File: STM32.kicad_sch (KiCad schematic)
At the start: 7 parts

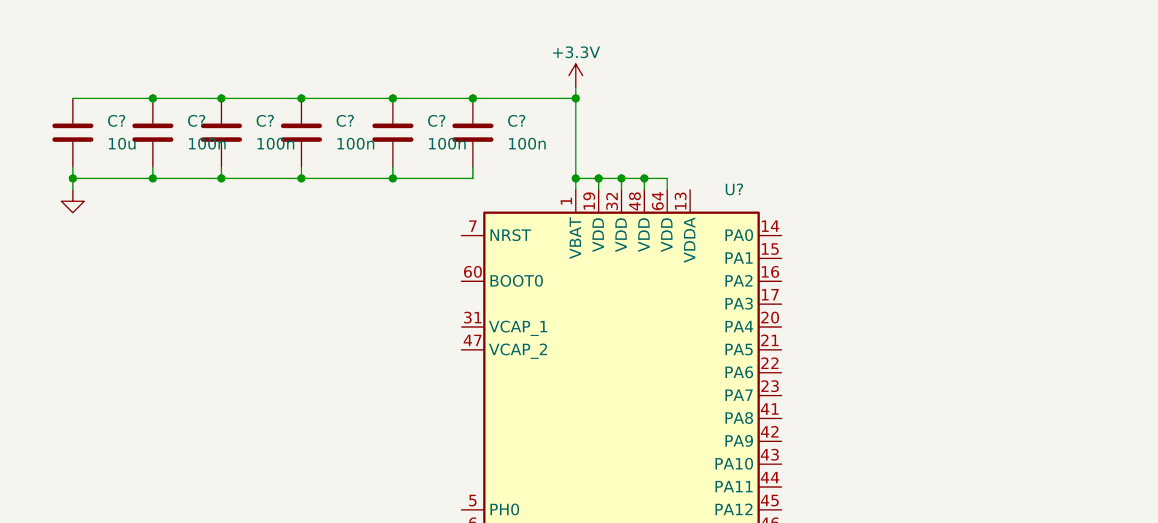
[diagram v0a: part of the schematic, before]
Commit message: update
NRST and BOOT0
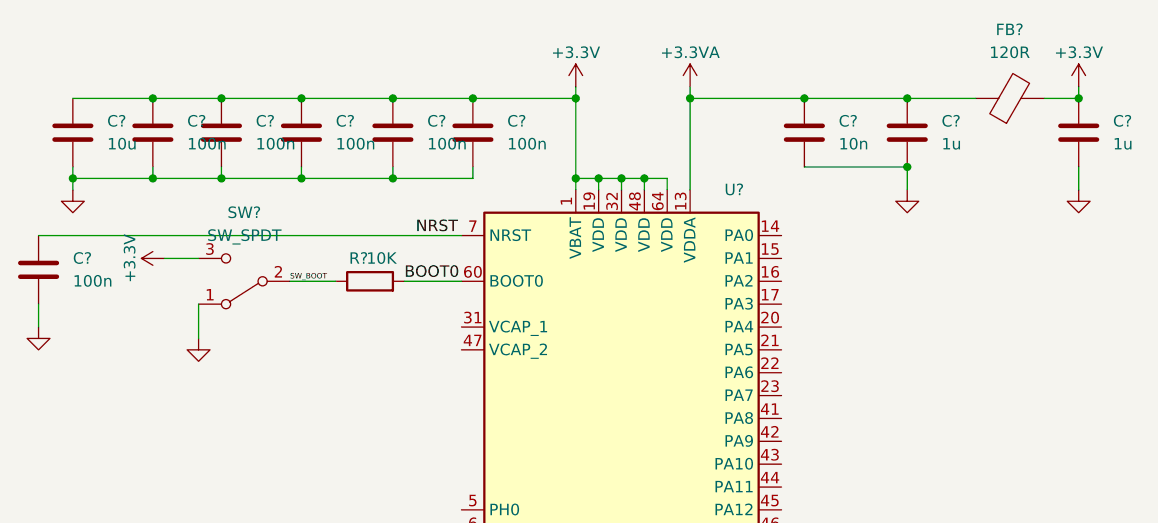
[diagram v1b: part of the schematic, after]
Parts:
- added C?: 10n, symbol Device:C
- added C? (x2): 1u, symbol Device:C
- added C?: 100n, symbol Device:C
- added FB?: 120R, symbol Device:FerriteBead
- added R?: 10K, symbol Device:R
- added SW?: SW_SPDT, symbol Switch:SW_SPDT
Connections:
- net +3.3V: now also C?.1, FB?.2, SW?.3 (C)
- net GND: now also C?.2, C?.2, C?.2, C?.2, SW?.1 (A)
- net +3.3VA: now reaches U?.13 (VDDA)
- net +3.3VA: now also C?.1, C?.1, FB?.1
- net BOOT0: now reaches U?.60 (BOOT0)
- net BOOT0: now also R?.2
- net NRST: now reaches U?.7 (NRST)
- net NRST: now also C?.1
- new net SW_BOOT: R?.1, SW?.2 (B)

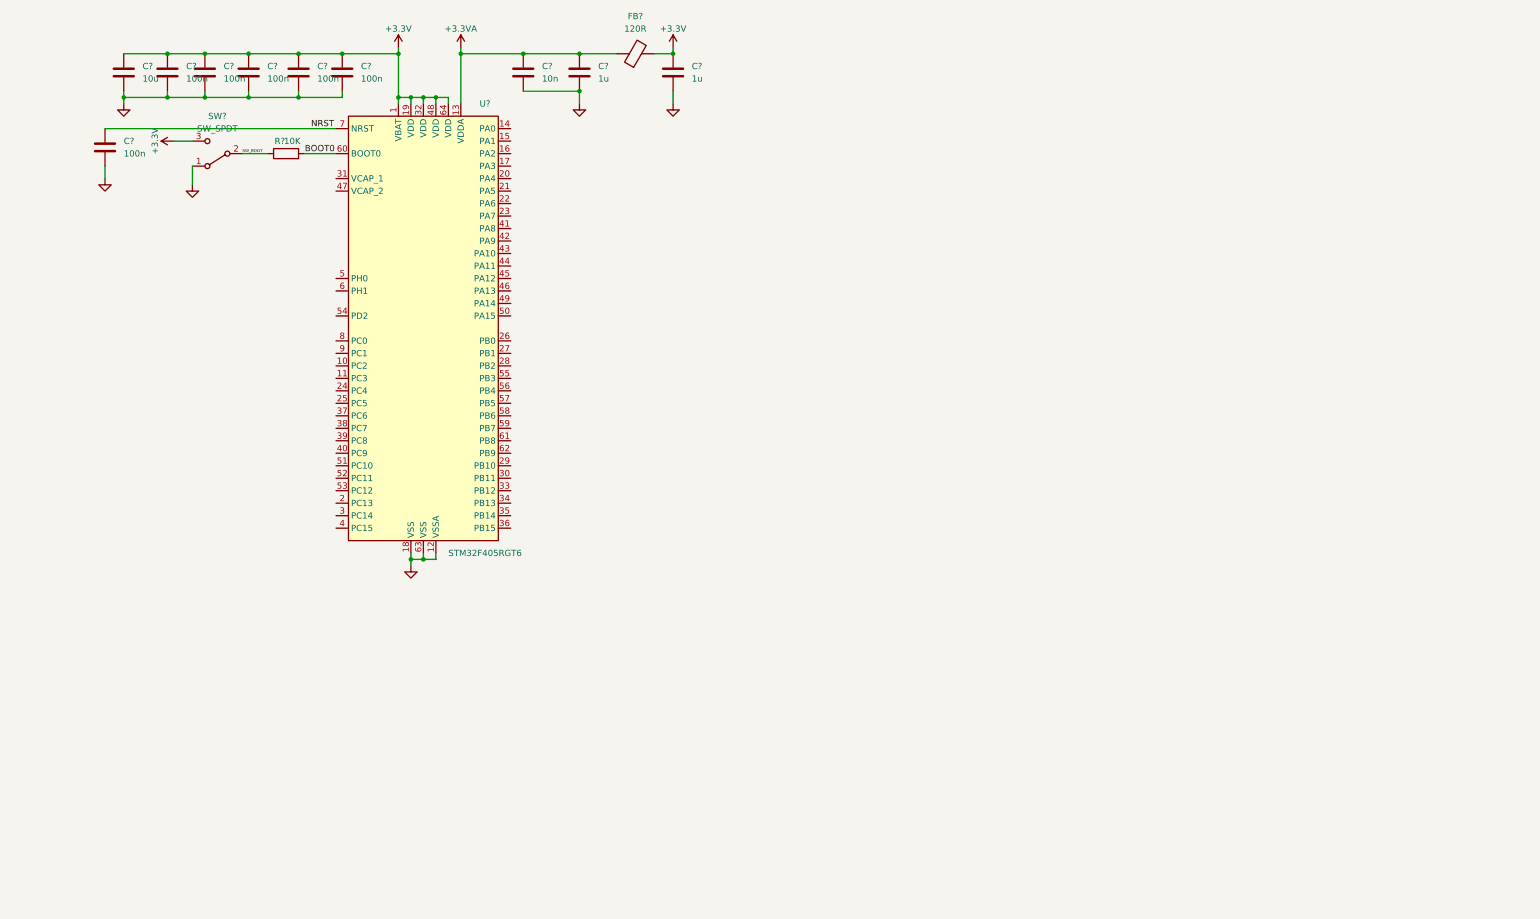
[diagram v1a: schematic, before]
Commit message: Schematics update
New files and schematics
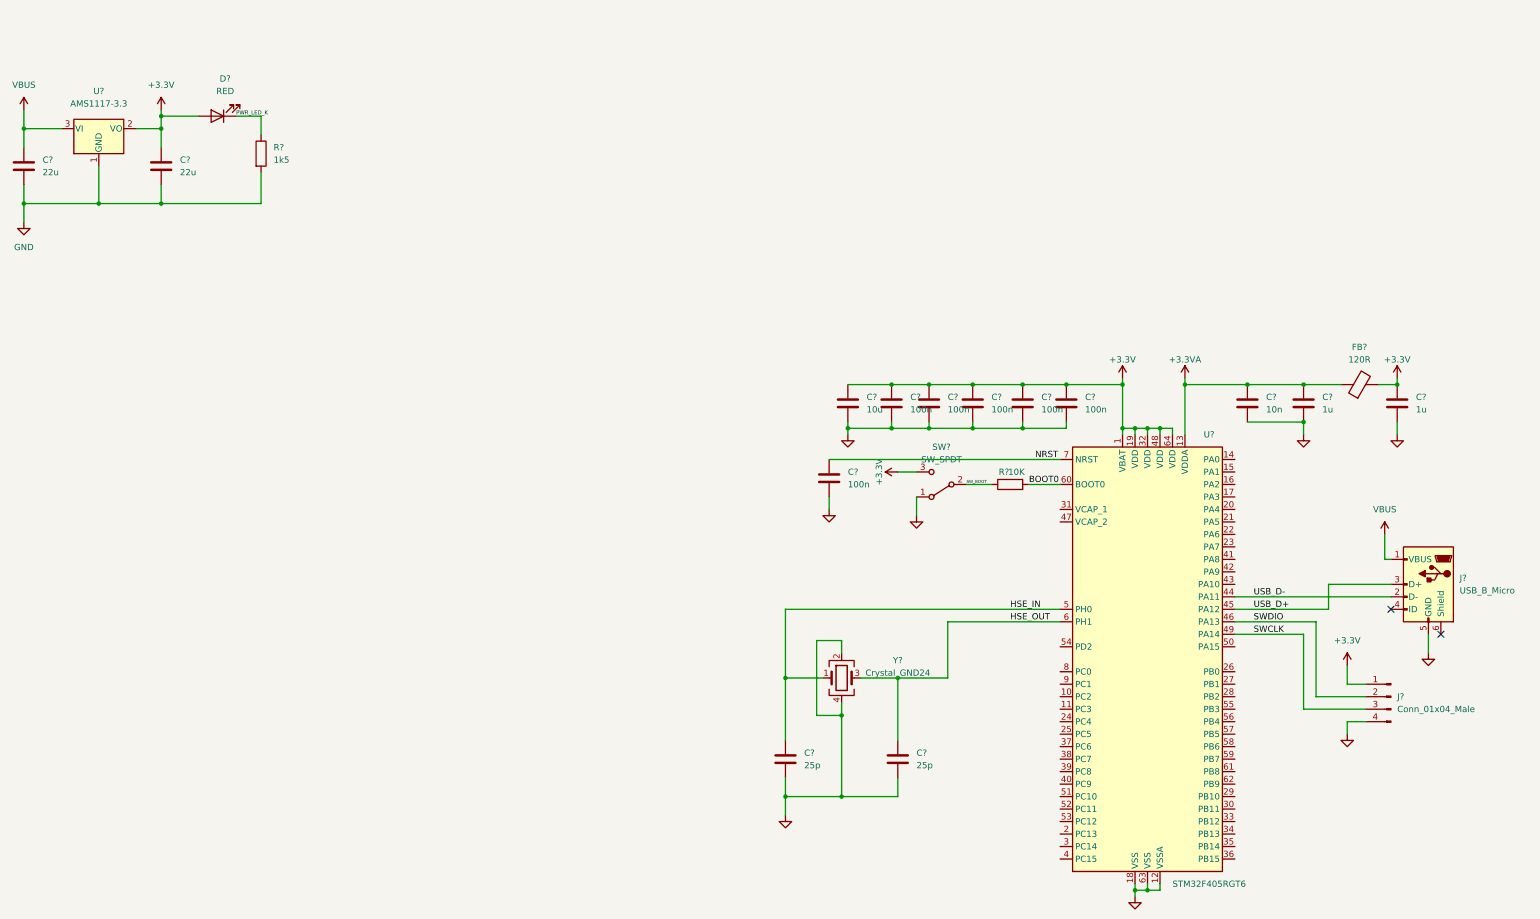
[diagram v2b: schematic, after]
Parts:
- added C? (x2): 22u, symbol Device:C
- added C? (x2): 25p, symbol Device:C
- added D?: RED, symbol Device:LED
- added J?: USB_B_Micro, symbol Connector:USB_B_Micro
- added J?: Conn_01x04_Male, symbol Connector:Conn_01x04_Male
- added R?: 1k5, symbol Device:R
- added U?: AMS1117-3.3, Package_TO_SOT_SMD:SOT-223-3_TabPin2, symbol Regulator_Linear:AMS1117-3.3
- added Y?: Crystal_GND24, symbol Device:Crystal_GND24
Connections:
- net +3.3V: now also C?.1, D?.2 (A), J?.1 (Pin_1), U?.2 (VO)
- net GND: now also C?.2, C?.2, C?.2, C?.2, J?.4 (Pin_4), J?.5 (GND), R?.2, U?.1 (GND), Y?.2, Y?.4
- net USB_D-: now reaches U?.44 (PA11)
- net USB_D-: now also J?.2 (D-)
- net USB_D+: now reaches U?.45 (PA12)
- net USB_D+: now also J?.3 (D+)
- net SWDIO: now reaches U?.46 (PA13)
- net SWDIO: now also J?.2 (Pin_2)
- net SWCLK: now reaches U?.49 (PA14)
- net SWCLK: now also J?.3 (Pin_3)
- net HSE_IN: now reaches U?.5 (PH0)
- net HSE_IN: now also C?.1, Y?.1
- net HSE_OUT: now reaches U?.6 (PH1)
- net HSE_OUT: now also C?.1, Y?.3
- new net PWR_LED_K: D?.1 (K), R?.1
- new net VBUS: C?.1, J?.1 (VBUS), U?.3 (VI)
- no-connect marks 0 -> 2
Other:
- moved on the sheet: C?, FB?, R?, SW?, U?

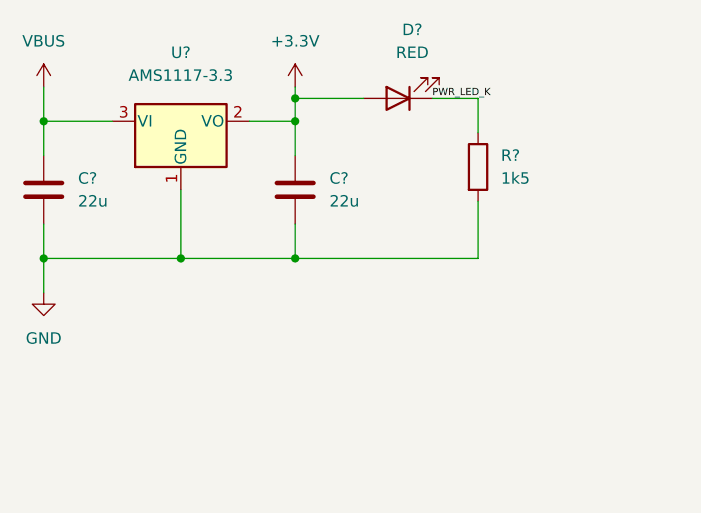
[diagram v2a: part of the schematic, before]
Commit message: Update STM32.kicad_sch
changes
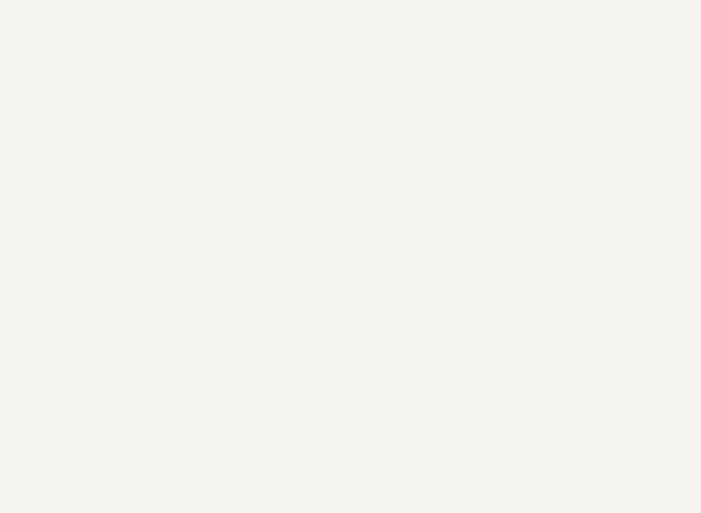
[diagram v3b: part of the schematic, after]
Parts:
- removed C? (x2): 22u, symbol Device:C
- removed D?: RED, symbol Device:LED
- removed R?: 1k5, symbol Device:R
- removed U?: AMS1117-3.3, Package_TO_SOT_SMD:SOT-223-3_TabPin2, symbol Regulator_Linear:AMS1117-3.3

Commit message: Update STM32.kicad_sch
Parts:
- added C? (x2): 2u2, symbol Device:C_Small
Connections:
- net GND: now also C?.2, C?.2
- net at U?.31 (VCAP_1): now also C?.1
- net at U?.47 (VCAP_2): now also C?.1
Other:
- moved on the sheet: C?, Y?

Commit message: change
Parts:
- removed C?: 1u, symbol Device:C
- removed FB?: 120R, symbol Device:FerriteBead
- added L?: 39u, symbol Device:L_Small
- C?: value 10u -> 4u7
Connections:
- net +3.3V: now also C?.1, C?.1, L?.2
- net +3.3VA: now also L?.1; no longer C?.1, C?.1
- net LED_STATUS: now reaches U?.16 (PA2)
- net I2C2_SCL: now reaches U?.29 (PB10)
- net I2C2_SDA: now reaches U?.30 (PB11)
- net UART3_TX: now reaches U?.51 (PC10)
- net UART3_RX: now reaches U?.52 (PC11)
- net SWO: now reaches U?.55 (PB3)
- net I2C1_SCL: now reaches U?.58 (PB6)
- net I2C1_SDA: now reaches U?.59 (PB7)
- no-connect marks 2 -> 40

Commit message: changes
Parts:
- added 47u: R_Small, symbol Device:R_Small
- gave numbers to parts that had none: 1
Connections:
- net HSE_OUT: now also 47u.2; no longer 16Mhz.3, C?.1
- new net: 16Mhz.3, 47u.1, C?.1
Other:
- moved on the sheet: 16Mhz, C?, J?, L?, R?, SW?, U?

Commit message: update
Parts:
- removed 16Mhz: Crystal_GND24, symbol Device:Crystal_GND24
- removed R?: 10K, symbol Device:R
- added 16Mhz: Crystal_GND24_Small, symbol Device:Crystal_GND24_Small
- added D?: Green, symbol Device:LED_Small
- added R? (x2): 10k, symbol Device:R_Small
- added U?: MP2359DJ-LF-Z, symbol Kronos:MP2359DJ-LF-Z
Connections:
- net BOOT0: now also R?.2
- net GND: now also 16Mhz.2, 16Mhz.4, R?.2, U?.2 (GND)
- net HSE_IN: now also 16Mhz.1
- net LED_STATUS: now also D?.2 (A)
- net SW_BOOT: now also R?.1
- net at 47u.1, C?.1: now also 16Mhz.3
- new net: D?.1 (K), R?.1
- new net BUCK_BST: U?.1 (BST)
- new net BUCK_EN: U?.4 (EN)
- new net BUCK_FB: U?.3 (FB)
- new net BUCK_IN: U?.5 (IN)
- new net BUCK_SW: U?.6 (SW)
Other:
- note added: "STM32 MCU"
- company: (none) -> Kronos
- title: (none) -> STM32F4RGT6
- moved on the sheet: 47u, C?, J?, L?, SW?, U?

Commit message: pc
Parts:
- removed C?: 100n, symbol Device:C
- removed J?: USB_B_Micro, symbol Connector:USB_B_Micro
- removed J?: Conn_01x04_Male, symbol Connector:Conn_01x04_Male
- added C?: 10u, symbol Device:C
- added C? (x2): 10u, symbol Device:C_Small
- added C?: 10n, symbol Device:C
- added D? (x2): B5819W, symbol Device:D_Schottky_Small
- added F?: 250mA, symbol Device:Polyfuse_Small
- added FB?: 600 @ 600MHz, symbol Device:FerriteBead_Small
- added J?: SWD, symbol Connector_Generic:Conn_02x05_Odd_Even
- added J?: Screw_Terminal_01x02, symbol Connector:Screw_Terminal_01x02
- added J?: USB_B_Micro, symbol Connector:USB_B_Micro
- added L?: 10u, symbol Device:L_Small
- added Q?: AO3401A, Package_TO_SOT_SMD:SOT-23, symbol Transistor_FET:AO3401A
- added R? (x2): 15k, symbol Device:R_Small
- added R?: 68k, symbol Device:R_Small
- added R?: 100k, symbol Device:R_Small
- added R?: 270, symbol Device:R_Small
- added R?: 47k, symbol Device:R_Small
- added U?: USBLC6-2SC6, Package_TO_SOT_SMD:SOT-23-6, symbol Power_Protection:USBLC6-2SC6
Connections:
- net +3.3V: now also C?.1, C?.1, J?.1 (Pin_1), L?.2, R?.1
- net BUCK_BST: now also C?.1
- net BUCK_EN: now also R?.1, R?.2
- net BUCK_FB: now also R?.1, R?.2
- net BUCK_IN: now also C?.1, FB?.1, R?.1
- net BUCK_SW: now also C?.2, D?.1 (K), L?.1
- net GND: now also C?.2, C?.2, C?.2, D?.2 (A), J?.2 (Pin_2), J?.3 (Pin_3), J?.5 (GND), J?.5 (Pin_5), J?.9 (Pin_9), Q?.1 (G), R?.2, R?.2, U?.2 (GND)
- net NRST: now also J?.10 (Pin_10)
- net SWCLK: now also J?.4 (Pin_4)
- net SWDIO: now also R?.1
- net SWO: now also J?.6 (Pin_6)
- net USB_D+: now also U?.4 (I/O2)
- net USB_D-: now also U?.6 (I/O1)
- new net: J?.2 (Pin_2), R?.2
- new net: R?.1, R?.2
- new net: D?.1 (K), FB?.2, Q?.2 (S)
- new net: F?.2, Q?.3 (D)
- new net +12V: F?.1, J?.1 (Pin_1)
- new net +5V: D?.2 (A), J?.1 (VBUS), U?.5 (VBUS)
- new net USB_CONN_D+: J?.3 (D+), U?.3 (I/O2)
- new net USB_CONN_D-: J?.2 (D-), U?.1 (I/O1)
- no-connect marks 40 -> 42
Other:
- moved on the sheet: U?
